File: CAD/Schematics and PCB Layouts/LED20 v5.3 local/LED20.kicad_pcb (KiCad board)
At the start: 2 copper layers, 30 x 35 mm, 35 parts, among them U3 MMBT4401LT1G, U6 B2B-PH-K-S, U7 B2B-PH-K-S

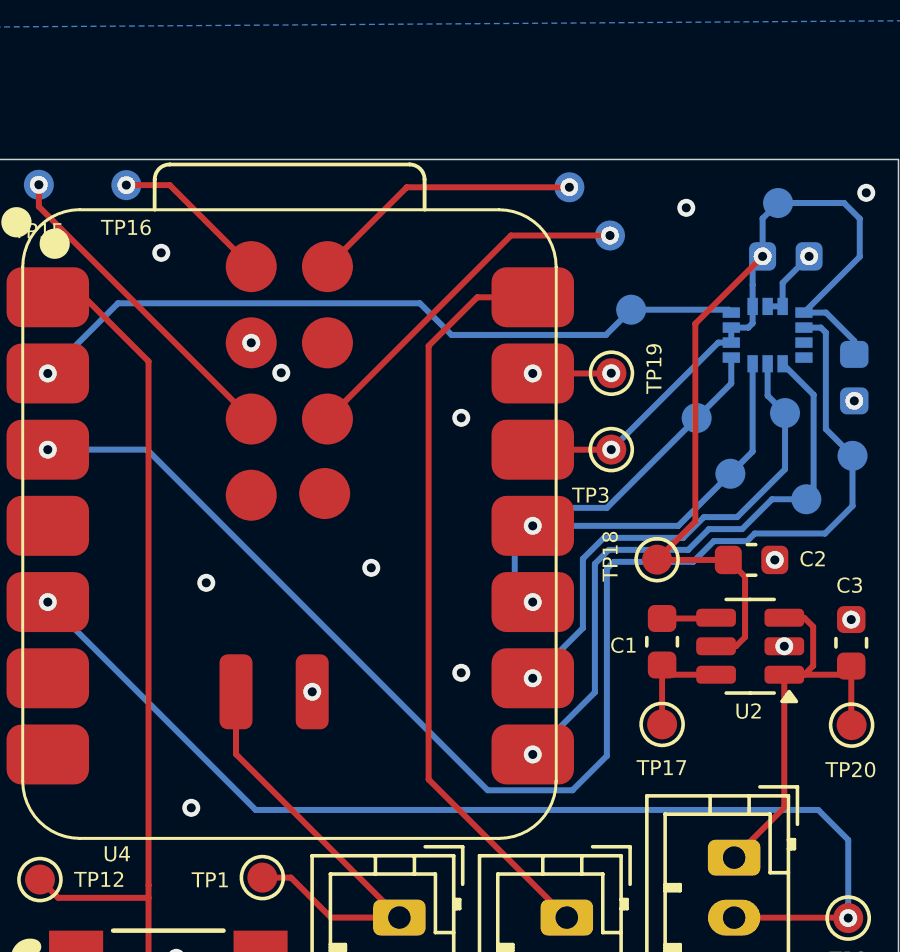
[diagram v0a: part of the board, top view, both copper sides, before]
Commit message: Updated PCB
added 2.1mm mounting hole. Seems quite large may have clearance issues.
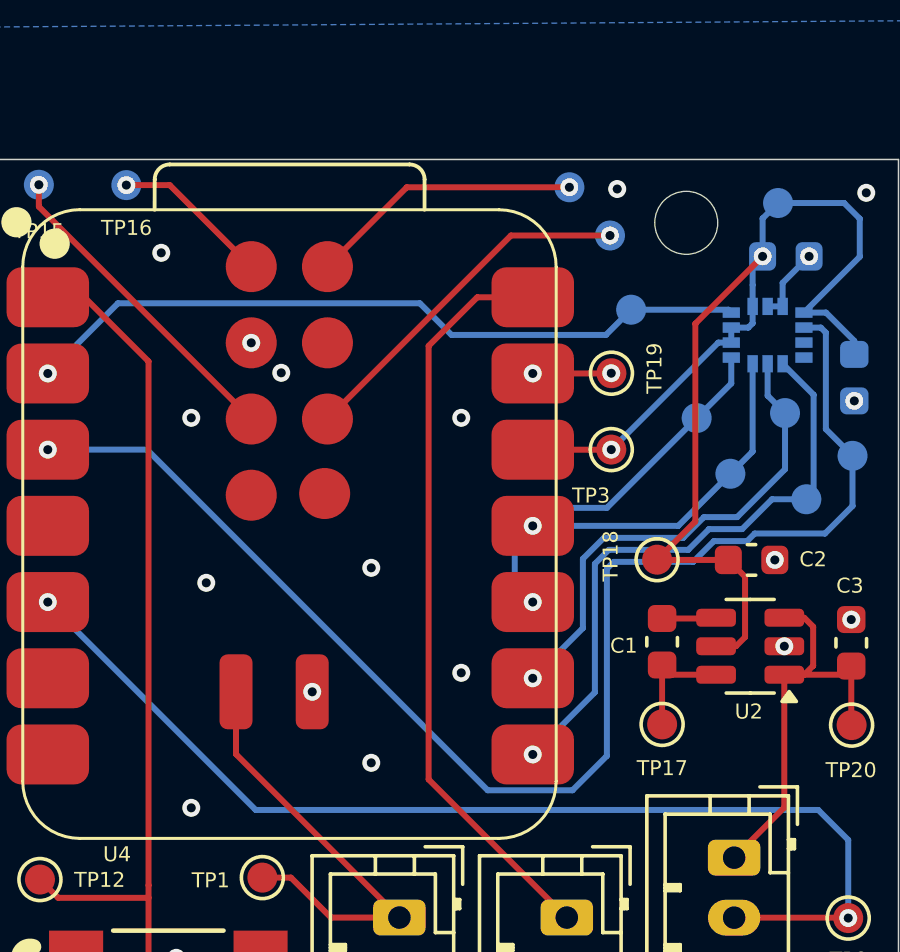
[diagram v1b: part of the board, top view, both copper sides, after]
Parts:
- added REF**: MountingHole_2.1mm, MountingHole:MountingHole_2.1mm, B.Cu at (155.1, 65.5)
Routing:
- net GND: vias 22 -> 24
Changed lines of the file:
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@@
 		)
 		(property "Footprint" "Footprints:SMA_403AE_OSI"
-			(at 0 0 360)
+			(at 0 0 0)
 			(layer "F.Fab")
 			(hide yes)
@@
 		)
 		(property "Datasheet" "S1B"
-			(at 0 0 360)
+			(at 0 0 0)
 			(layer "F.Fab")
 			(hide yes)
@@
 		)
 		(property "Description" ""
-			(at 0 0 360)
+			(at 0 0 0)
 			(layer "F.Fab")
 			(hide yes)
@@
 		(tags "resistor")
 		(property "Reference" "R1"
-			(at 0 -1.43 360)
+			(at 0 -1.43 0)
 			(layer "F.SilkS")
 			(effects
@@
 		)
 		(property "Value" "180"
-			(at 0 1.43 360)
+			(at 0 1.43 0)
 			(layer "F.Fab")
 			(effects
@@
 		)
 		(fp_text user "${REFERENCE}"
-			(at 0 0 360)
+			(at 0 0 0)
 			(layer "F.Fab")
 			(effects
@@
 		)
 	)
+	(footprint "MountingHole:MountingHole_2.1mm"
+		(layer "B.Cu")
+		(at 155.1375 65.45 180)
+		(descr "Mounting Hole 2.1mm, no annular")
+		(tags "mounting hole 2.1mm no annular")
+		(property "Reference" "REF**"
+			(at 0 4 0)
+			(layer "B.SilkS")
+			(hide yes)
+			(effects
+				(font
+					(size 1 1)
+					(thickness 0.15)
+				)
+				(justify mirror)
+			)
+		)
+		(property "Value" "MountingHole_2.1mm"
+			(at 0 -3.2 0)
+			(layer "B.Fab")
+			(effects
+				(font
+					(size 1 1)
+					(thickness 0.15)
+				)
+				(justify mirror)
+			)
+		)
+		(property "Footprint" "MountingHole:MountingHole_2.1mm"
+			(at 0 0 0)
+			(unlocked yes)
+			(layer "B.Fab")
+			(hide yes)
+			(effects
+				(font
+					(size 1.27 1.27)
+					(thickness 0.15)
+				)
+				(justify mirror)
+			)
+		)
+		(property "Datasheet" ""
+			(at 0 0 0)
+			(unlocked yes)
+			(layer "B.Fab")
+			(hide yes)
+			(effects
+				(font
+					(size 1.27 1.27)
+					(thickness 0.15)
+				)
+				(justify mirror)
+			)
+		)
+		(property "Description" ""
+			(at 0 0 0)
+			(unlocked yes)
+			(layer "B.Fab")
+			(hide yes)
+			(effects
+				(font
+					(size 1.27 1.27)
+					(thickness 0.15)
+				)
+				(justify mirror)
+			)
+		)
+		(attr exclude_from_pos_files exclude_from_bom)
+		(fp_circle
+			(center 0 0)
+			(end 2.1 0)
+			(stroke
+				(width 0.15)
+				(type solid)
+			)
+			(fill none)
+			(layer "Cmts.User")
+		)
+		(fp_circle
+			(center 0 0)
+			(end 2.35 0)
+			(stroke
+				(width 0.05)
+				(type solid)
+			)
+			(fill none)
+			(layer "B.CrtYd")
+		)
+		(fp_text user "${REFERENCE}"
+			(at 0 0 0)
+			(layer "B.Fab")
+			(effects
+				(font
+					(size 1 1)
+					(thickness 0.15)
+				)
+				(justify mirror)
+			)
+		)
+		(pad "" np_thru_hole circle
+			(at 0 0 180)
+			(size 2.1 2.1)
+			(drill 2.1)
+			(layers "*.Cu" "*.Mask")
+		)
+	)
 	(footprint "TestPoint:TestPoint_Pad_D1.0mm"
 		(layer "B.Cu")
@@
 	)
 	(via
-		(at 155.1375 64.95)
+		(at 152.835891 64.32261)
 		(size 0.6)
 		(drill 0.3)
@@
 	)
 	(via
+		(at 144.6375 83.45)
+		(size 0.6)
+		(drill 0.3)
+		(layers "F.Cu" "B.Cu")
+		(free yes)
+		(net 3)
+	)
+	(via
 		(at 143.1375 96.45)
 		(size 0.6)
@@
 		(net 3)
 	)
+	(via
+		(at 138.6375 71.95)
+		(size 0.6)
+		(drill 0.3)
+		(layers "F.Cu" "B.Cu")
+		(free yes)
+		(net 3)
+	)
